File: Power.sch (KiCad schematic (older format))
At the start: 24 parts, among them U13 L78L12_SOT89, U14 MP4560_QFN10, U3 L78L12_SOT89, U4 LP2985-3.3

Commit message: More routing
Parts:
- C70: footprint Capacitor_SMD:C_0603_1608Metric -> Capacitor_SMD:C_0402_1005Metric
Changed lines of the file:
@@
 F 0 "C70" V 6700 4500 50  0000 L CNN
 F 1 "0.1uF" V 6800 4500 50  0000 L CNN
-F 2 "Capacitor_SMD:C_0603_1608Metric" H 6900 4500 50  0001 C CNN
+F 2 "Capacitor_SMD:C_0402_1005Metric" H 6900 4500 50  0001 C CNN
 F 3 "~" H 6900 4500 50  0001 C CNN
 	1    6900 4500

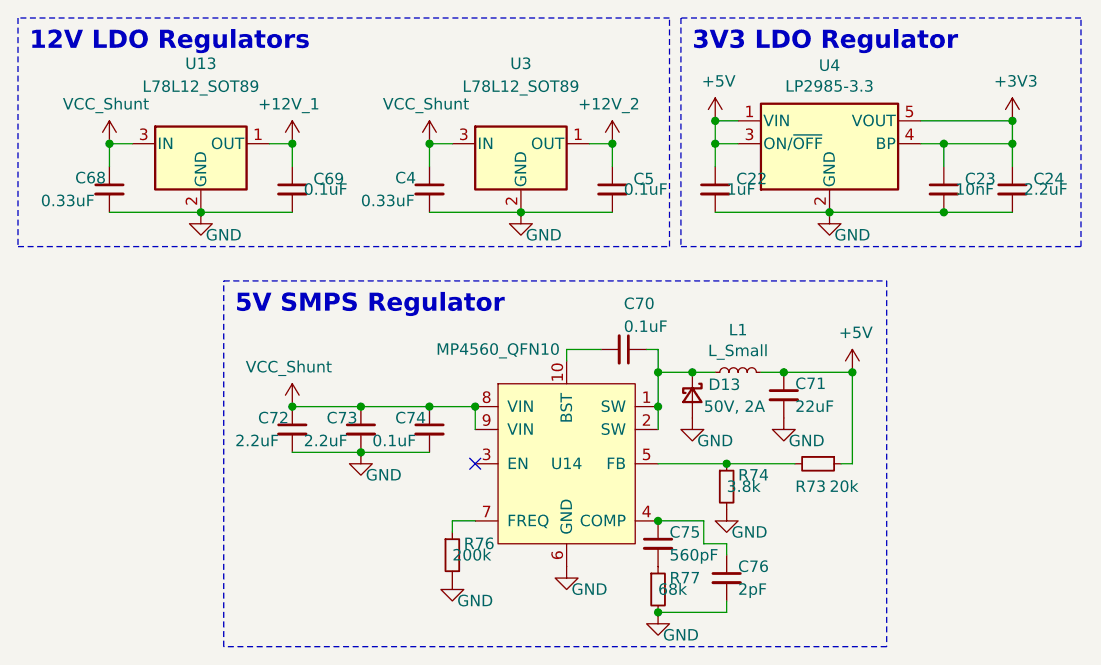
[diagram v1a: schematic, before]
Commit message: Started adding filtering caps
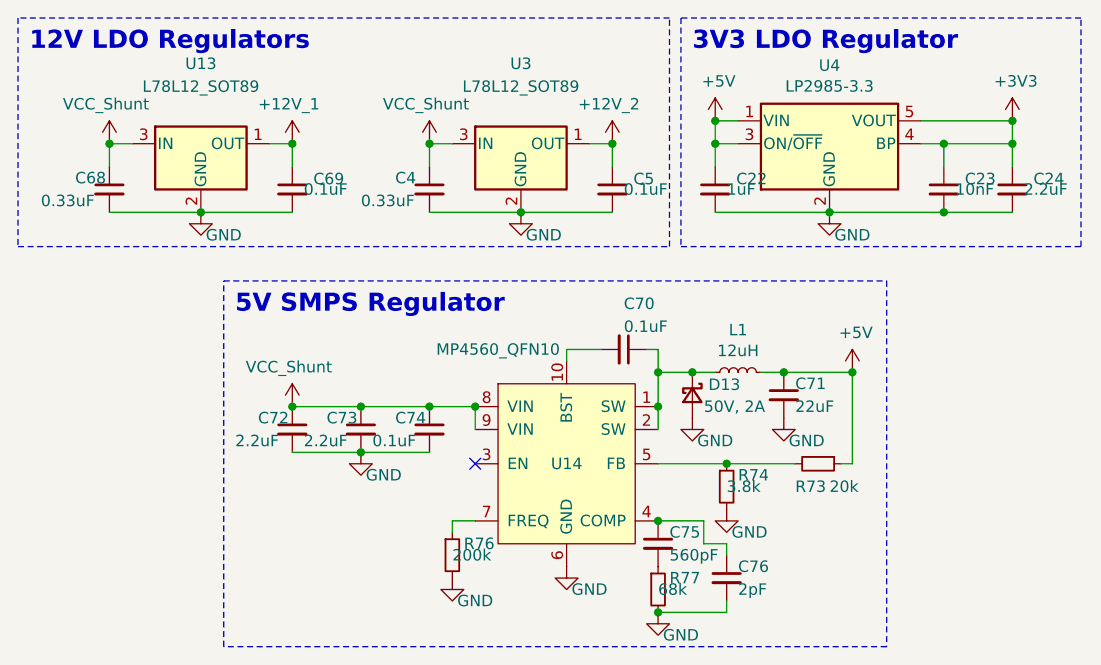
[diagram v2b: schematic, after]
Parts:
- L1: value L_Small -> 12uH; footprint Inductor_SMD:L_Bourns-SRN5020 -> Inductor_SMD:L_XGL4030
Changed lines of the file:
@@
 P 7400 4600
 F 0 "L1" V 7585 4600 50  0000 C CNN
-F 1 "L_Small" V 7494 4600 50  0000 C CNN
-F 2 "Inductor_SMD:L_Bourns-SRN5020" H 7400 4600 50  0001 C CNN
+F 1 "12uH" V 7494 4600 50  0000 C CNN
+F 2 "Inductor_SMD:L_XGL4030" H 7400 4600 50  0001 C CNN
 F 3 "~" H 7400 4600 50  0001 C CNN
 	1    7400 4600

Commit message: More routing done
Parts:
- U13, U3: footprint Package_TO_SOT_SMD:SOT-89-3 -> Footprints:L78L12ACUTR
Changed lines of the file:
@@
 F 0 "U3" H 6450 3950 50  0000 C CNN
 F 1 "L78L12_SOT89" H 6450 3850 50  0000 C CNN
-F 2 "Package_TO_SOT_SMD:SOT-89-3" H 6450 3800 50  0001 C CIN
+F 2 "Footprints:L78L12ACUTR" H 6450 3800 50  0001 C CIN
 F 3 "http://www.st.com/content/ccc/resource/technical/document/datasheet/15/55/e5/aa/23/5b/43/fd/CD00000446.pdf/files/CD00000446.pdf/jcr:content/translations/en.CD00000446.pdf" H 6450 3550 50  0001 C CNN
 	1    6450 3600
@@
 F 0 "U13" H 5050 3950 50  0000 C CNN
 F 1 "L78L12_SOT89" H 5050 3850 50  0000 C CNN
-F 2 "Package_TO_SOT_SMD:SOT-89-3" H 5050 3800 50  0001 C CIN
+F 2 "Footprints:L78L12ACUTR" H 5050 3800 50  0001 C CIN
 F 3 "http://www.st.com/content/ccc/resource/technical/document/datasheet/15/55/e5/aa/23/5b/43/fd/CD00000446.pdf/files/CD00000446.pdf/jcr:content/translations/en.CD00000446.pdf" H 5050 3550 50  0001 C CNN
 	1    5050 3600

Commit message: Added stuff
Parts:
- C4, C68: Notes (none) -> VCC Rated
- C5, C69: Notes (none) -> 12V Rated
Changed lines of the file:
@@
 F 2 "Capacitor_SMD:C_0603_1608Metric" H 6050 3800 50  0001 C CNN
 F 3 "~" H 6050 3800 50  0001 C CNN
+F 4 "VCC Rated" H 6050 3800 50  0001 C CNN "Notes"
 	1    6050 3800
 	1    0    0    -1
@@
 F 2 "Capacitor_SMD:C_0603_1608Metric" H 6850 3800 50  0001 C CNN
 F 3 "~" H 6850 3800 50  0001 C CNN
+F 4 "12V Rated" H 6850 3800 50  0001 C CNN "Notes"
 	1    6850 3800
 	1    0    0    -1
@@
 F 2 "Capacitor_SMD:C_0603_1608Metric" H 4650 3800 50  0001 C CNN
 F 3 "~" H 4650 3800 50  0001 C CNN
+F 4 "VCC Rated" H 4650 3800 50  0001 C CNN "Notes"
 	1    4650 3800
 	1    0    0    -1
@@
 F 2 "Capacitor_SMD:C_0603_1608Metric" H 5450 3800 50  0001 C CNN
 F 3 "~" H 5450 3800 50  0001 C CNN
+F 4 "12V Rated" H 5450 3800 50  0001 C CNN "Notes"
 	1    5450 3800
 	1    0    0    -1
